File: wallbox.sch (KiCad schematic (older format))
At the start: 36 parts, among them J1 From Transformer, J2 To Wallbox, J3 To Microcontroller, Q1 BC547, Q2 BC547, Q3 BC547, U1 KA78R33, U2 LM7805CT, U3 TPC817MC, U4 TPC817MC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

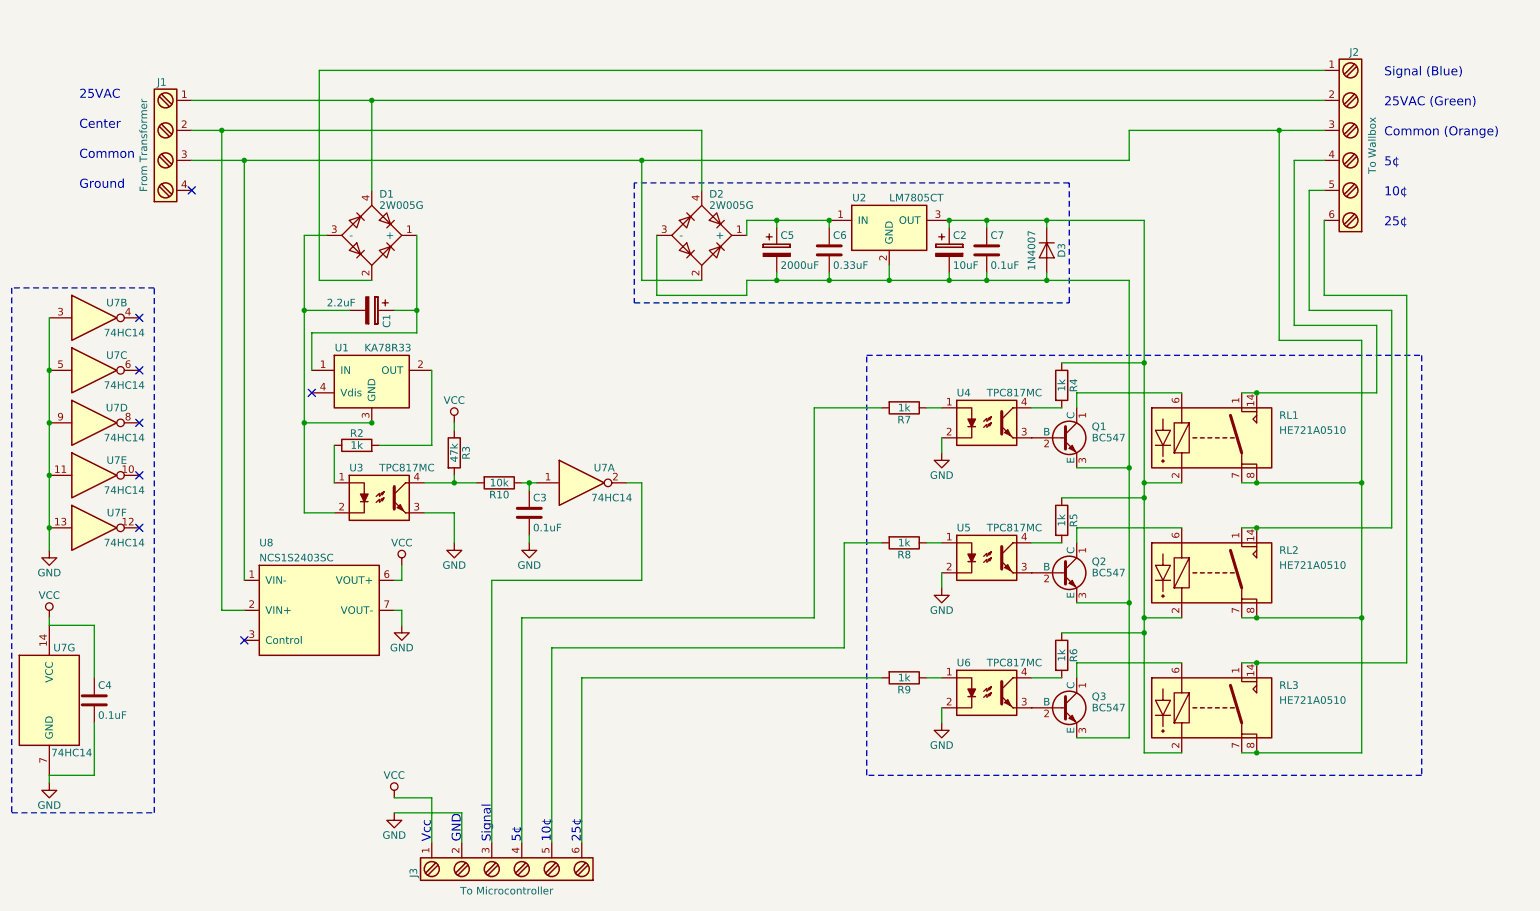
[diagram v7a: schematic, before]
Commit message: Add block descriptions
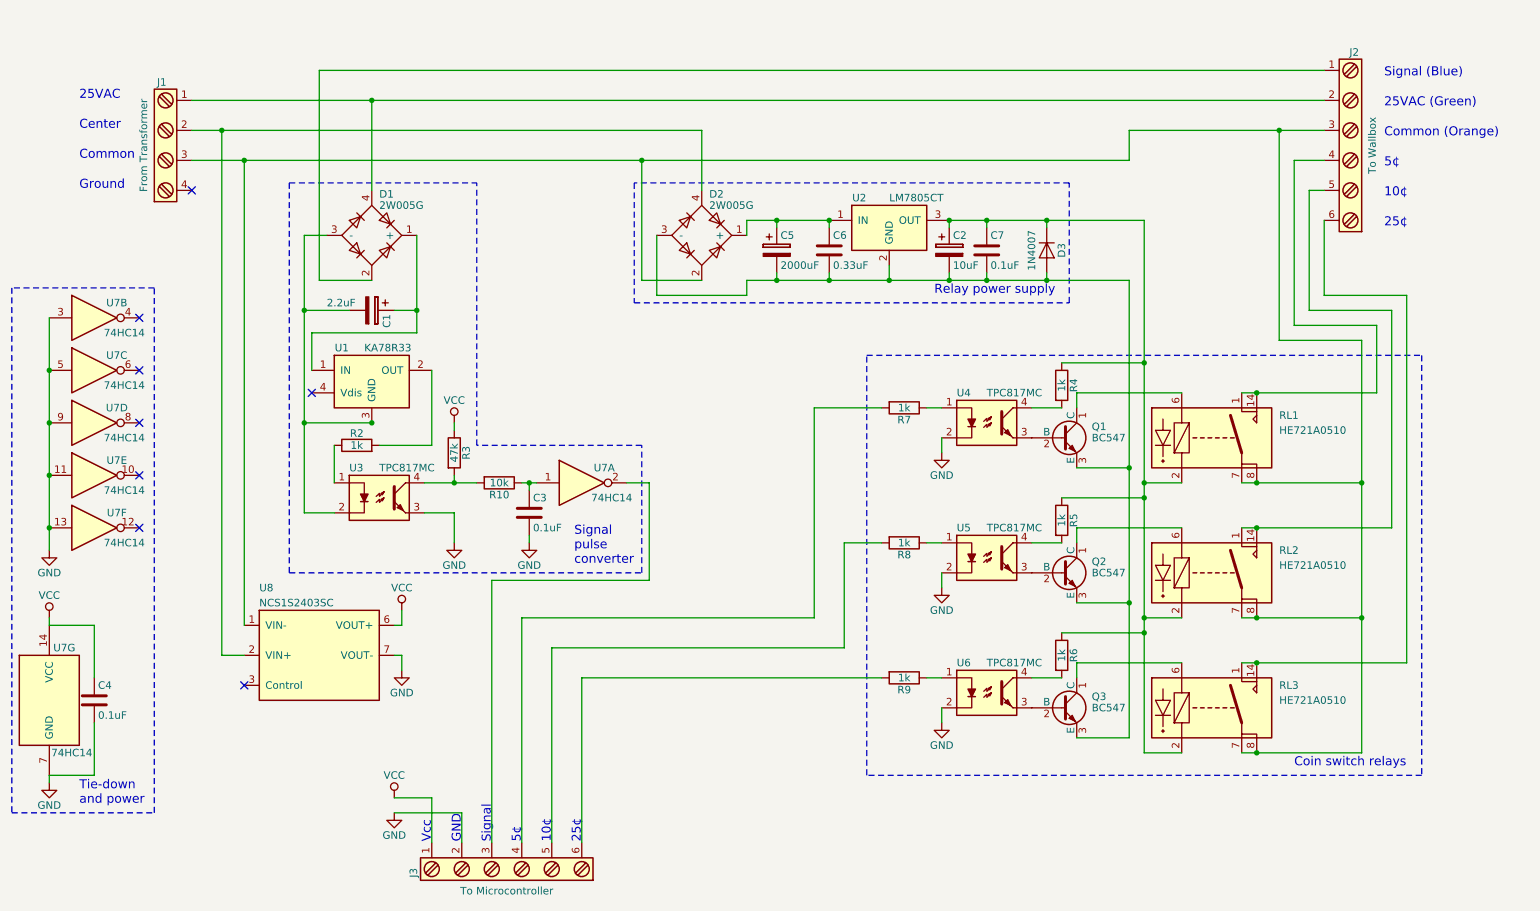
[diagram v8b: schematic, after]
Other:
- note added: "Coin switch relays"
- note added: "Relay power supply"
- note added: "Signal\npulse\nconverter"
- note added: "Tie-down\nand power"
- moved on the sheet: U8
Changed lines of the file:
@@
 L NCS1S2403SC U8
 U 1 1 59DFE027
-P 2550 4700
-F 0 "U8" H 2150 5150 50  0000 L CNN
-F 1 "NCS1S2403SC" H 2150 5050 50  0000 L CNN
-F 2 "" H 3150 4300 50  0001 C CIN
-F 3 "" H 2550 4700 50  0001 C CNN
-	1    2550 4700
-	1    0    0    -1
-$EndComp
-NoConn ~ 2050 4900
+P 2550 5000
+F 0 "U8" H 2150 5450 50  0000 L CNN
+F 1 "NCS1S2403SC" H 2150 5350 50  0000 L CNN
+F 2 "" H 3150 4600 50  0001 C CIN
+F 3 "" H 2550 5000 50  0001 C CNN
+	1    2550 5000
+	1    0    0    -1
+$EndComp
+NoConn ~ 2050 5200
 $Comp
 L VCC #PWR07
 U 1 1 59DFFC00
-P 3100 4400
-F 0 "#PWR07" H 3100 4250 50  0001 C CNN
-F 1 "VCC" H 3100 4550 50  0000 C CNN
-F 2 "" H 3100 4400 50  0001 C CNN
-F 3 "" H 3100 4400 50  0001 C CNN
-	1    3100 4400
+P 3100 4700
+F 0 "#PWR07" H 3100 4550 50  0001 C CNN
+F 1 "VCC" H 3100 4850 50  0000 C CNN
+F 2 "" H 3100 4700 50  0001 C CNN
+F 3 "" H 3100 4700 50  0001 C CNN
+	1    3100 4700
 	1    0    0    -1
 $EndComp
@@
 L GND #PWR08
 U 1 1 59DFFC89
-P 3100 4800
-F 0 "#PWR08" H 3100 4550 50  0001 C CNN
-F 1 "GND" H 3100 4650 50  0000 C CNN
-F 2 "" H 3100 4800 50  0001 C CNN
-F 3 "" H 3100 4800 50  0001 C CNN
-	1    3100 4800
+P 3100 5100
+F 0 "#PWR08" H 3100 4850 50  0001 C CNN
+F 1 "GND" H 3100 4950 50  0000 C CNN
+F 2 "" H 3100 5100 50  0001 C CNN
+F 3 "" H 3100 5100 50  0001 C CNN
+	1    3100 5100
 	1    0    0    -1
 $EndComp
@@
 	1450 2550 500  2550
 Wire Wire Line
-	2050 4500 2050 1700
+	2050 4800 2050 1700
 Connection ~ 2050 1700
 Wire Wire Line
-	2050 4700 1900 4700
-Wire Wire Line
-	1900 4700 1900 1500
+	2050 5000 1900 5000
+Wire Wire Line
+	1900 5000 1900 1500
 Connection ~ 1900 1500
 Wire Wire Line
-	3050 4500 3100 4500
-Wire Wire Line
-	3100 4500 3100 4400
-Wire Wire Line
-	3050 4700 3100 4700
-Wire Wire Line
-	3100 4700 3100 4800
+	3050 4800 3100 4800
+Wire Wire Line
+	3100 4800 3100 4700
+Wire Wire Line
+	3050 5000 3100 5000
+Wire Wire Line
+	3100 5000 3100 5100
 Wire Notes Line
 	4650 1850 4650 2650
@@
 	7550 1850 4650 1850
 Wire Wire Line
-	4600 3850 4700 3850
-Wire Wire Line
-	4700 3850 4700 4500
-Wire Wire Line
-	4700 4500 3700 4500
+	4600 3850 4750 3850
+Wire Wire Line
+	4750 3850 4750 4500
+Wire Wire Line
+	4750 4500 3700 4500
 Wire Wire Line
 	3700 4500 3700 6250
@@
 	9250 2600 9800 2600
 Wire Wire Line
-	9800 2600 9800 5050
-Wire Wire Line
-	9800 5050 8700 5050
+	9800 5050 9800 2600
+Wire Wire Line
+	8700 5050 9800 5050
 Wire Wire Line
 	9250 1900 9150 1900
@@
 	9150 2700 9700 2700
 Wire Wire Line
-	9700 2700 9700 4150
-Wire Wire Line
-	9700 4150 8700 4150
+	9700 4150 9700 2700
+Wire Wire Line
+	8700 4150 9700 4150
 Wire Wire Line
 	9250 1700 9050 1700
@@
 	9050 2800 9600 2800
 Wire Wire Line
-	9600 2800 9600 3250
-Wire Wire Line
-	9600 3250 8700 3250
+	9600 3250 9600 2800
+Wire Wire Line
+	8700 3250 9600 3250
 Connection ~ 8800 3250
 Connection ~ 8800 4150
@@
 	8950 2900 9500 2900
 Wire Wire Line
-	9500 2900 9500 5650
-Wire Wire Line
-	9500 5650 8700 5650
+	9500 5650 9500 2900
+Wire Wire Line
+	8700 5650 9500 5650
 Connection ~ 8950 1500
 Wire Wire Line
@@
 Connection ~ 8800 4750
 Connection ~ 8800 5650
+Wire Notes Line
+	2350 1850 3600 1850
+Wire Notes Line
+	2350 1850 2350 4450
+Wire Notes Line
+	2350 4450 4700 4450
+Wire Notes Line
+	4700 4450 4700 3600
+Wire Notes Line
+	4700 3600 3600 3600
+Wire Notes Line
+	3600 3600 3600 1850
+Text Notes 4250 4400 0    60   ~ 0
+Signal\npulse\nconverter
+Text Notes 6650 2600 0    60   ~ 0
+Relay power supply
+Text Notes 9050 5750 0    60   ~ 0
+Coin switch relays
+Text Notes 950  6000 0    60   ~ 0
+Tie-down\nand power
 $EndSCHEMATC
